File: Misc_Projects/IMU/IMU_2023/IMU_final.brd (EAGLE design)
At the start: 20.3 x 22.9 mm, 6 parts, among them IC1 ISM330DHCXTR

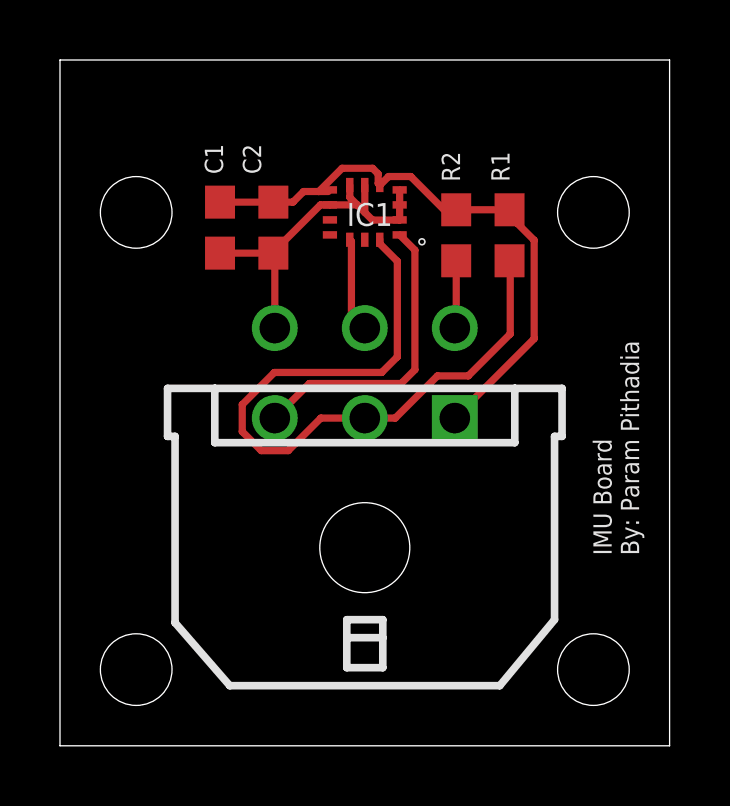
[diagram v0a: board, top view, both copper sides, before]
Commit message: Finished IMU board
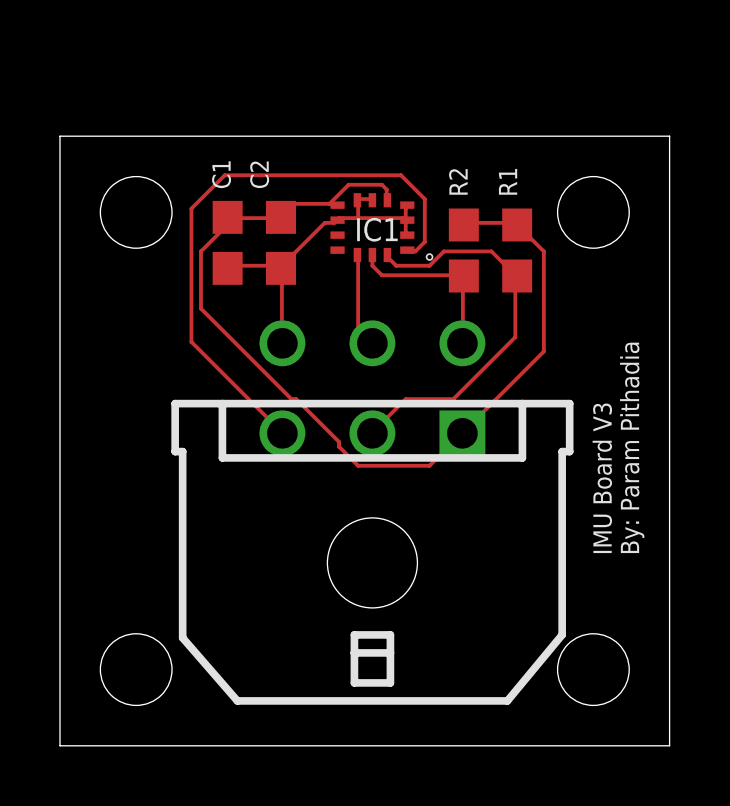
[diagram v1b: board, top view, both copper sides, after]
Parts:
- moved IC1 0.57 mm to (10.4, 17.3)
- moved X1 0.57 mm to (10.4, 6.10)
- moved C1 0.57 mm to (5.59, 16.8)
- moved C2 0.57 mm to (7.37, 16.8)
- moved R1 0.57 mm to (15.2, 16.5)
- moved R2 0.57 mm to (13.5, 16.5)
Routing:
- net 3V3: track 19.9 -> 31.6 mm
- net SDA: track 24.1 -> 13.2 mm
- net SDO: track 10.0 -> 19.5 mm
- net SCL: track 2.26 -> 5.80 mm
- net GND: track 12.1 -> 11.5 mm
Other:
- board size 20.3 x 22.9 mm -> 20.3 x 20.3 mm
- board text added: "IMU Board V3 By: Param Pithadia"
- board text removed: "IMU Board By: Param Pithadia"
